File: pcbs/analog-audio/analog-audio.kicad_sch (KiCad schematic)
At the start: 37 parts, among them J1 AudioJack5, J2 PWR, J5 BASS, J6 TREBLE, J7 Channel, Q1 TIP31, Q2 TIP31, Q3 TIP32, Q4 TIP32, Q5 TIP32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

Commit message: re-designed for power
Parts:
- removed J2: PWR, TerminalBlock:TerminalBlock_bornier-3_P5.08mm, symbol Connector:Screw_Terminal_01x03
- added J2: 24VDC, Connector_BarrelJack:BarrelJack_GCT_DCJ200-10-A_Horizontal, symbol Connector:Barrel_Jack_MountingPin
- added R19, R20: 10k, Resistor_THT:R_Axial_DIN0207_L6.3mm_D2.5mm_P7.62mm_Horizontal, symbol Device:R
- C3, C4: value 10uF -> 1mF; footprint Capacitor_THT:C_Radial_D6.3mm_H11.0mm_P2.50mm -> Capacitor_THT:C_Radial_D10.0mm_H12.5mm_P5.00mm
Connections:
- net +12V: now also C3.1, J2.1, R19.1; no longer C4.1
- net -12V: now also C4.2, J2.2, J2.MP (MountPin), R20.2; no longer C3.2
- net GND: now also C3.2, C4.1, R19.2, R20.1; no longer C3.1, C4.2
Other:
- note added: "CLASS AB POWER AMPLIFIER Amplify signals to get up to 850 mA, 5.88 V (about 5 W) peak-to-peak. Based on: https://www.youtube.com/watch?v=YuVqccvgNPM"
- note added: "CROSSOVER FILTERS Filter low-pass (bass) and high-pass (treble). Cutoff frequency: 1326 Hz"
- note added: "POWER SUPPLY Split 24 V into +12 V and -12 V"
- note added: "SIGNAL INPUT Choose between left and right using a jumper"
- moved on the sheet: C1, C2, J1, J5, J6, J7, Q1, Q2, Q3, Q4, Q5, Q6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

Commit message: added volume control
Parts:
- added J3, J4: VOL, Connector_JST:JST_EH_B2B-EH-A_1x02_P2.50mm_Vertical, symbol Connector_Generic:Conn_01x02
- R3, R4: value 1k -> 820E
- R5, R6: value 6.2k -> 10k
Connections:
- net VHPF_PA: now also J3.1 (Pin_1)
- net VLPF_PA: now also J4.1 (Pin_1)
- net at R3.2, R6.1, U2.2 (-): now also J4.2 (Pin_2)
- net at R4.2, R5.1, U1.2 (-): now also J3.2 (Pin_2)
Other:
- moved on the sheet: R3, R6, U2

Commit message: clean up schematic
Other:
- note added: "CLASS AB POWER AMPLIFIER (BASS/LPF) Amplify signals to get up to 850 mA, 5.88 V (about 5 W) peak-to-peak. Based on: https://www.youtube.com/watch?v=YuVqccvgNPM"
- note added: "CLASS AB POWER AMPLIFIER (TREBLE/HPF) Amplify signals to get up to 850 mA, 5.88 V (about 5 W) peak-to-peak. Based on: https://www.youtube.com/watch?v=YuVqccvgNPM"
- note added: "Outputs to drivers (RL = 4E)"
- note added: "PRE-AMP (BASS/LPF) Voltage gain = 6 (approx) Use Rv = 10k pot for volume control g = 6 at Rv = 10k, g --> 0 as Rv --> 0"
- note added: "PRE-AMP (TREBLE/HPF) Voltage gain = 6 (approx) Use Rv = 10k pot for volume control g = 6 at Rv = 10k, g --> 0 as Rv --> 0"
- note removed: "CLASS AB POWER AMPLIFIER Amplify signals to get up to 850 mA, 5.88 V (about 5 W) peak-to-peak. Based on: https://www.youtube.com/watch?v=YuVqccvgNPM"
- title: (none) -> Speaker Amplifier
- moved on the sheet: C1, C2, J1, J3, J4, J5, J6, J7, Q1, Q2, Q3, Q4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

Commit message: successful sims?
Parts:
- added R21, R22: 10k, Resistor_THT:R_Axial_DIN0207_L6.3mm_D2.5mm_P7.62mm_Horizontal, symbol Device:R
- added RL_BASS1, RL_TREBLE1: ${SIM.PARAMS}, symbol Device:R
- added VS1: 24V, symbol Simulation_SPICE:VDC
- added V_PWR1: ${SIM.PARAMS}, symbol Simulation_SPICE:VDC
- R3, R4: value 820E -> 820R
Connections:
- net +12V: now also VS1.1
- net -12V: now also VS1.2
- net VBASS: now also RL_BASS1.1
- net VHPF_PA: now also R21.2
- net VLPF_PA: now also R22.2
- net VTREBLE: now also RL_TREBLE1.1
- net Vs: now also V_PWR1.1
- net at J4.2 (Pin_2), R3.2, R6.1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: now also R22.1
- net at J3.2 (Pin_2), R4.2, R5.1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: now also R21.1
- net GND renamed 0
- net 0: now also RL_BASS1.2, RL_TREBLE1.2, V_PWR1.2
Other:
- note added: "SPICE SIMULATION These components are not included in the PCB. For testing only."
- moved on the sheet: C1, C2, J3, J4, R1, R2, R3, R4, R5, R6, U1, U2

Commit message: successful sims!!
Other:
- moved on the sheet: J3, J4

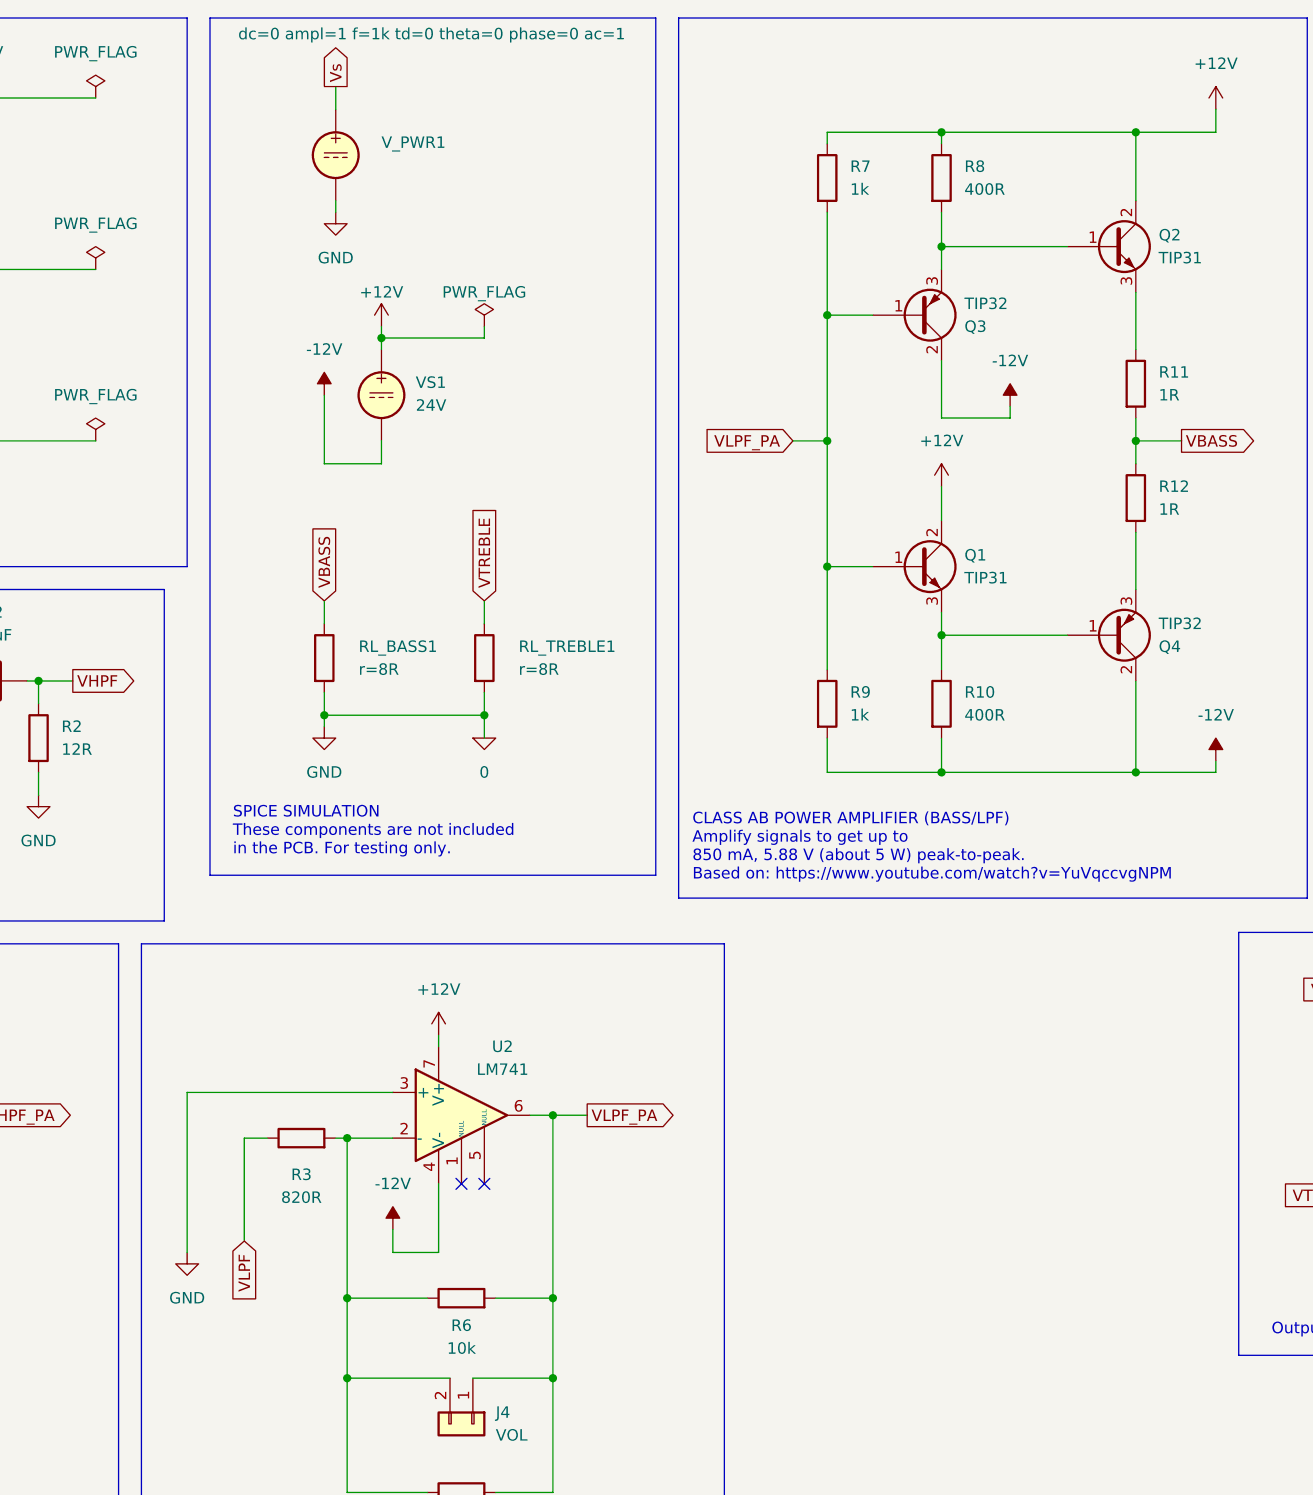
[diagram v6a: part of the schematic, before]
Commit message: add mounting holes
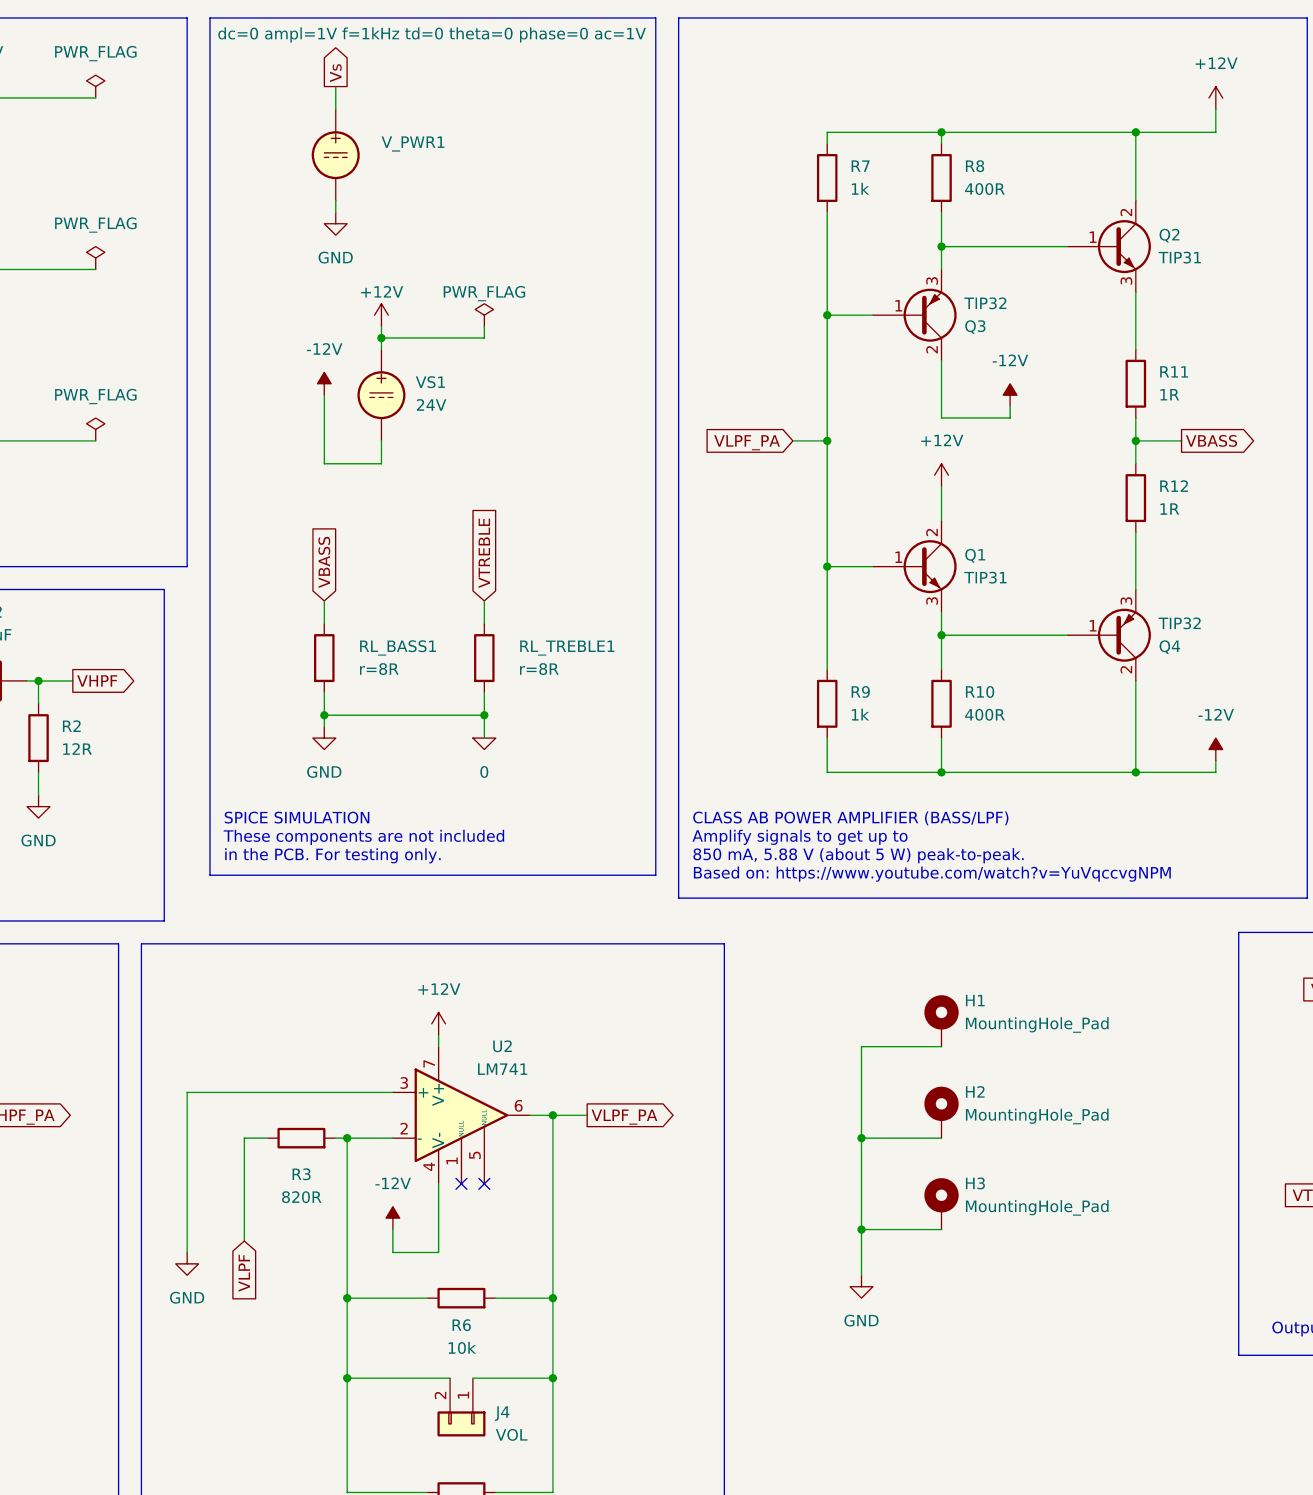
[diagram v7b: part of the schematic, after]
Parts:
- added H1, H2, H3: MountingHole_Pad, MountingHole:MountingHole_3.2mm_M3_Pad_Via, symbol Mechanical:MountingHole_Pad
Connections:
- net 0: now also H1.1, H2.1, H3.1

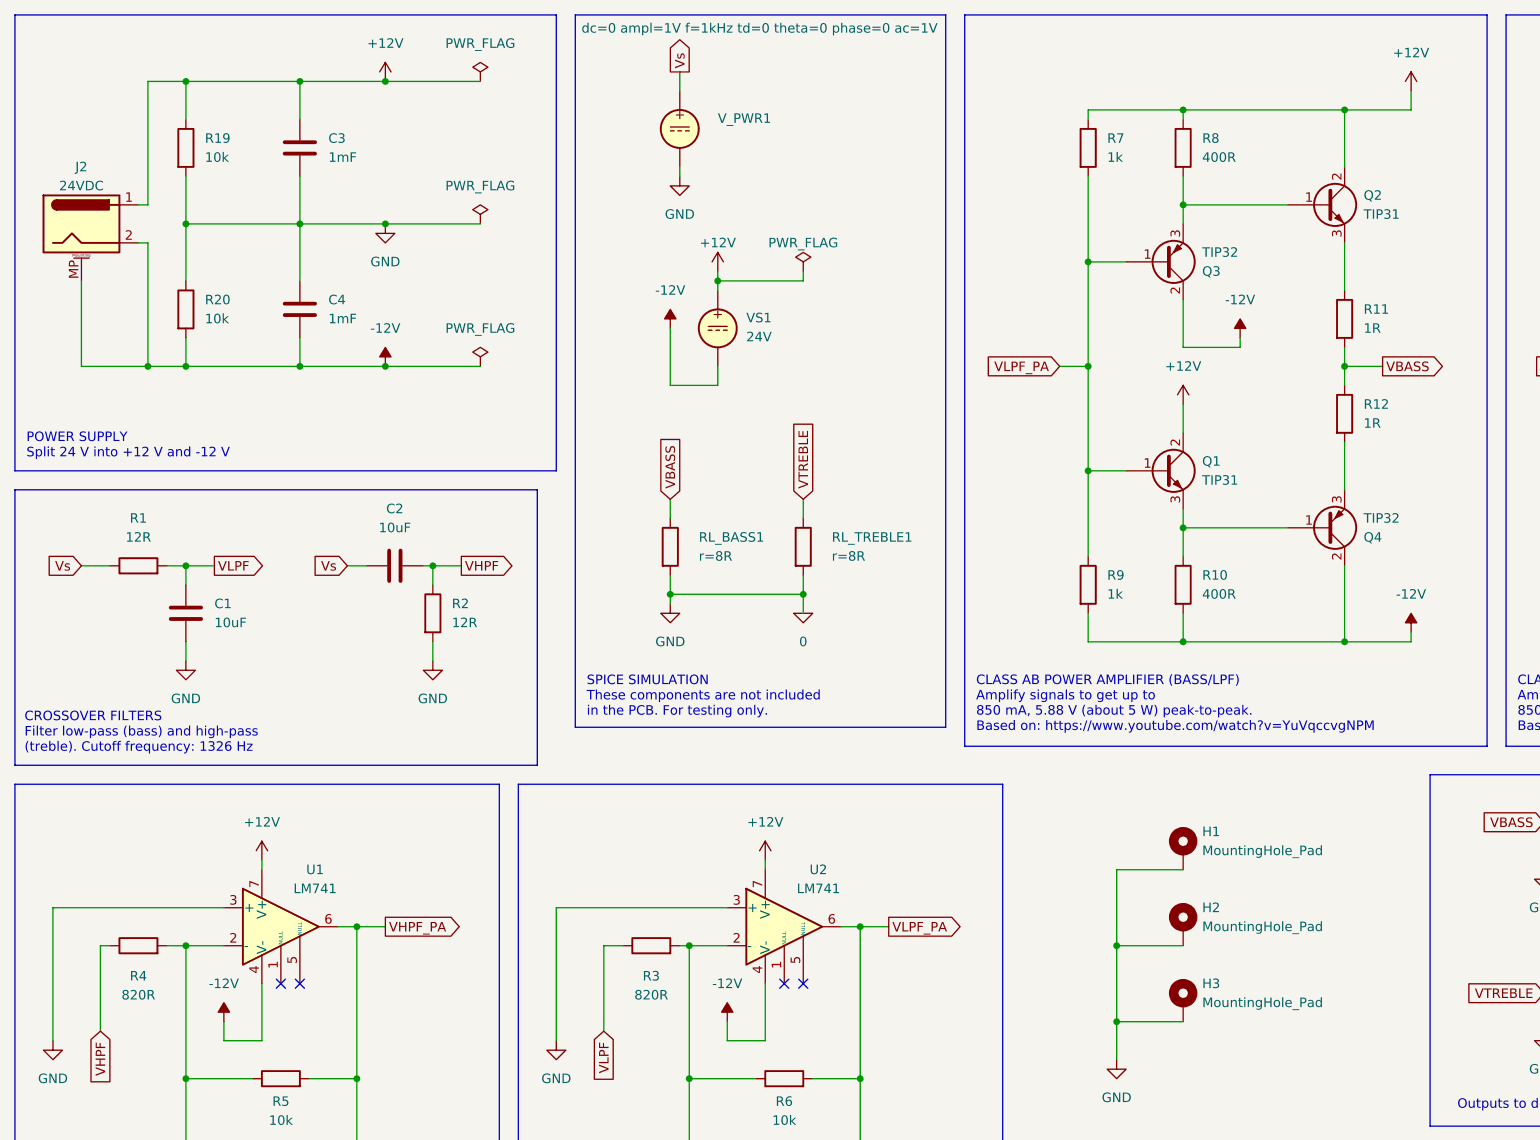
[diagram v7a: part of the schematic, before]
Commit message: fixed simulations and updated schematic for real values
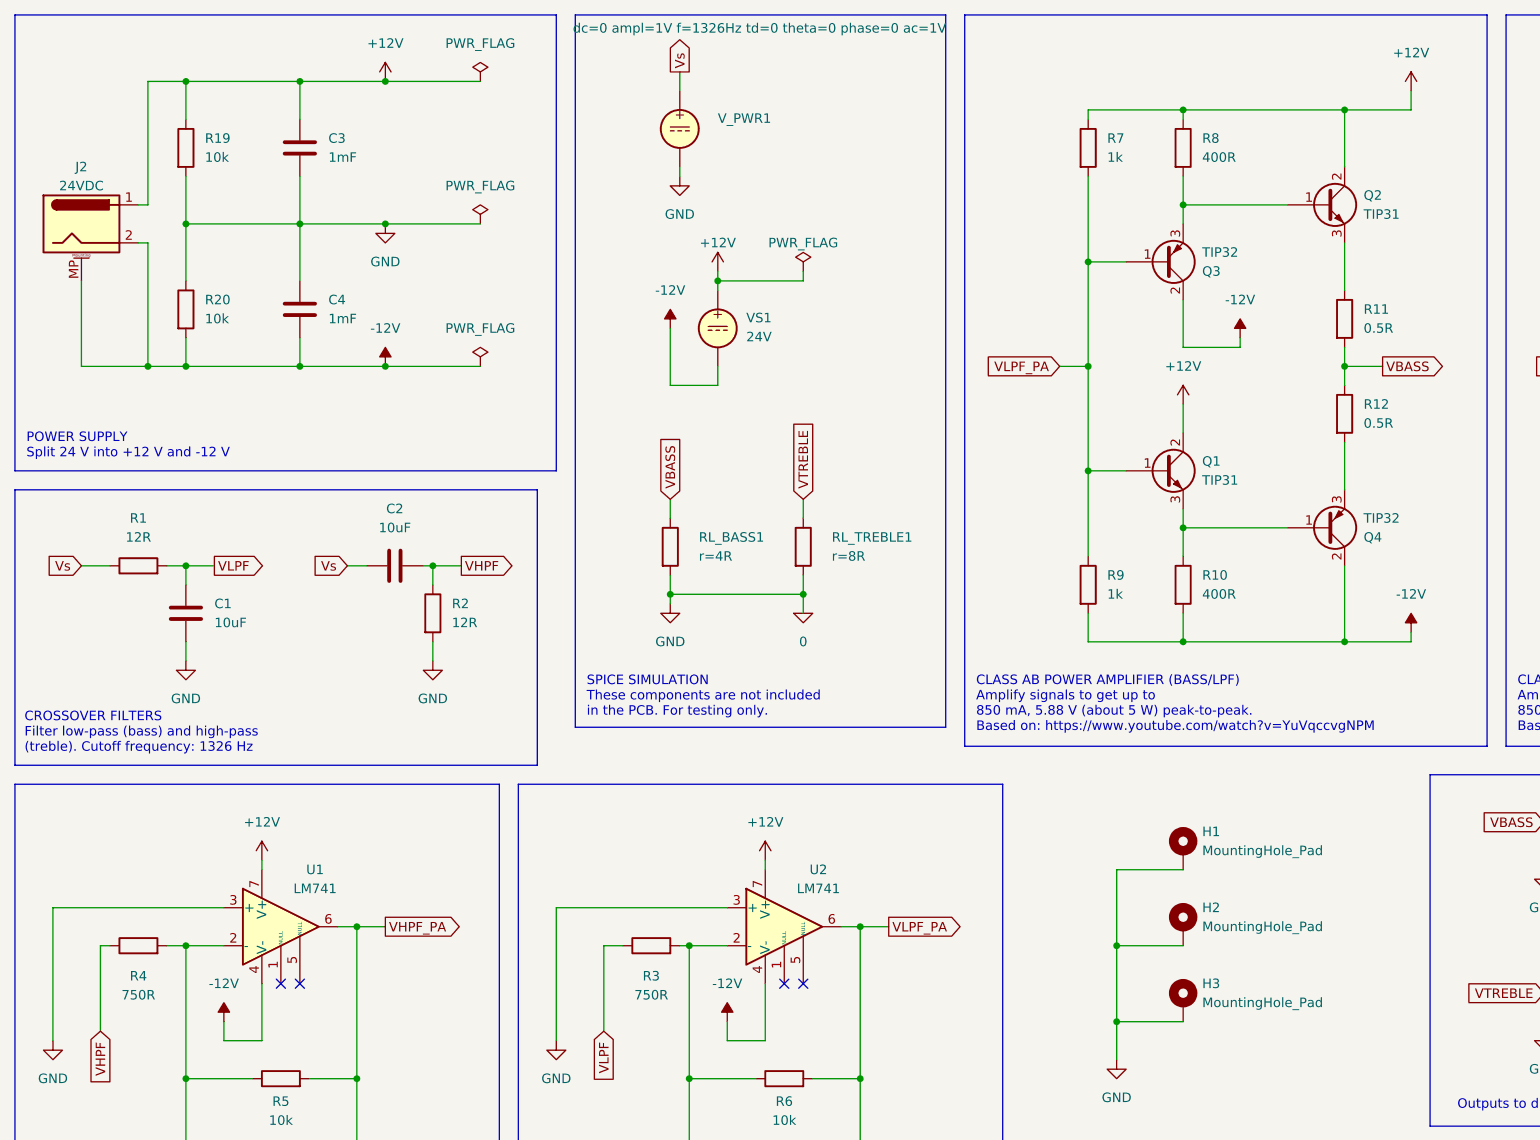
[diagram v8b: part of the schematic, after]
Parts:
- R11, R12: value 1R -> 0.5R
- R3, R4: value 820R -> 750R
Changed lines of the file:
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@@
 			)
 		)
-		(property "Sim.Params" "r=8R"
+		(property "Sim.Params" "r=4R"
 			(at 101.6 85.09 0)
 			(effects
@@
 			)
 		)
-		(property "Value" "820R"
+		(property "Value" "750R"
 			(at 99.06 145.034 90)
 			(effects
@@
 			)
 		)
-		(property "Value" "1R"
+		(property "Value" "0.5R"
 			(at 194.31 55.8799 0)
 			(effects
@@
 			)
 		)
-		(property "Value" "820R"
+		(property "Value" "750R"
 			(at 30.48 145.034 90)
 			(effects
@@
 			)
 		)
-		(property "Sim.Params" "dc=0 ampl=1V f=1kHz td=0 theta=0 phase=0 ac=1V"
+		(property "Sim.Params" "dc=0 ampl=1V f=1326Hz td=0 theta=0 phase=0 ac=1V"
 			(at 113.538 15.748 0)
 			(effects
@@
 			)
 		)
-		(property "Value" "1R"
+		(property "Value" "0.5R"
 			(at 194.31 68.5799 0)
 			(effects
